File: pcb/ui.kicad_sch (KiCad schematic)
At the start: 10 parts, among them Q1 2N7002, Q13 BSS84, Q14 BSS84, Q15 BSS84, Q16 BSS84, U18 NHD-C12864A1Z-FSW-FBW-HTT, U21 74LVC1G139, U23 74LVC1G139, U24 TLC5927IPWPR

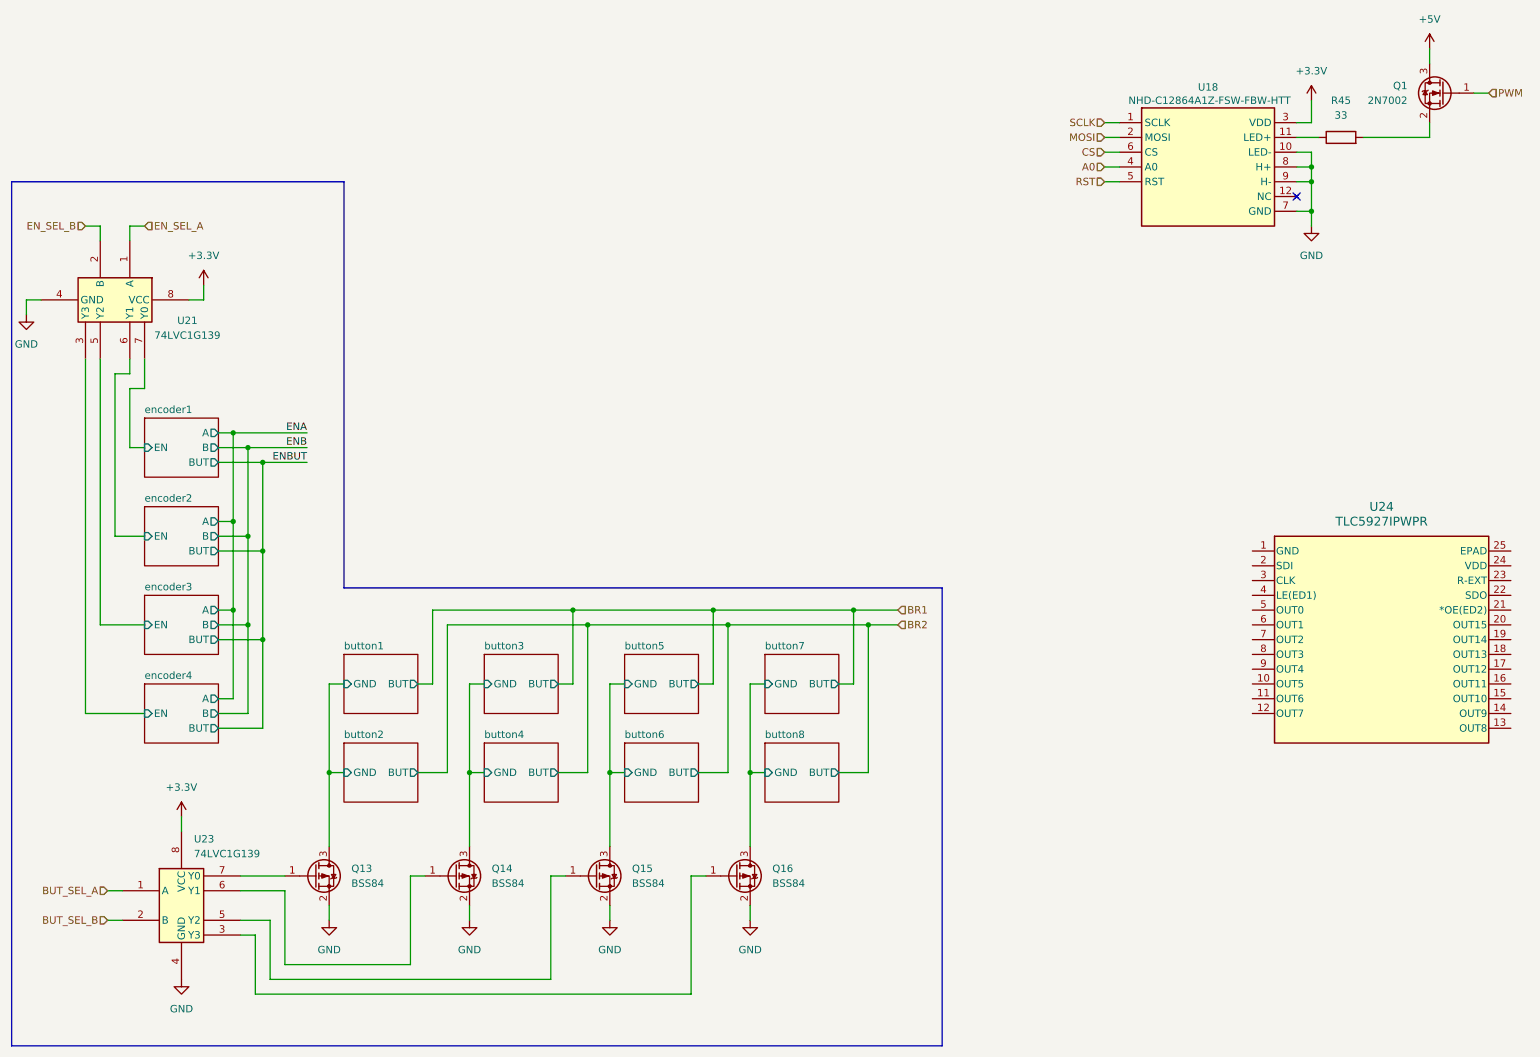
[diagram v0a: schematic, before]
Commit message: refactor: removed the laser component of the project
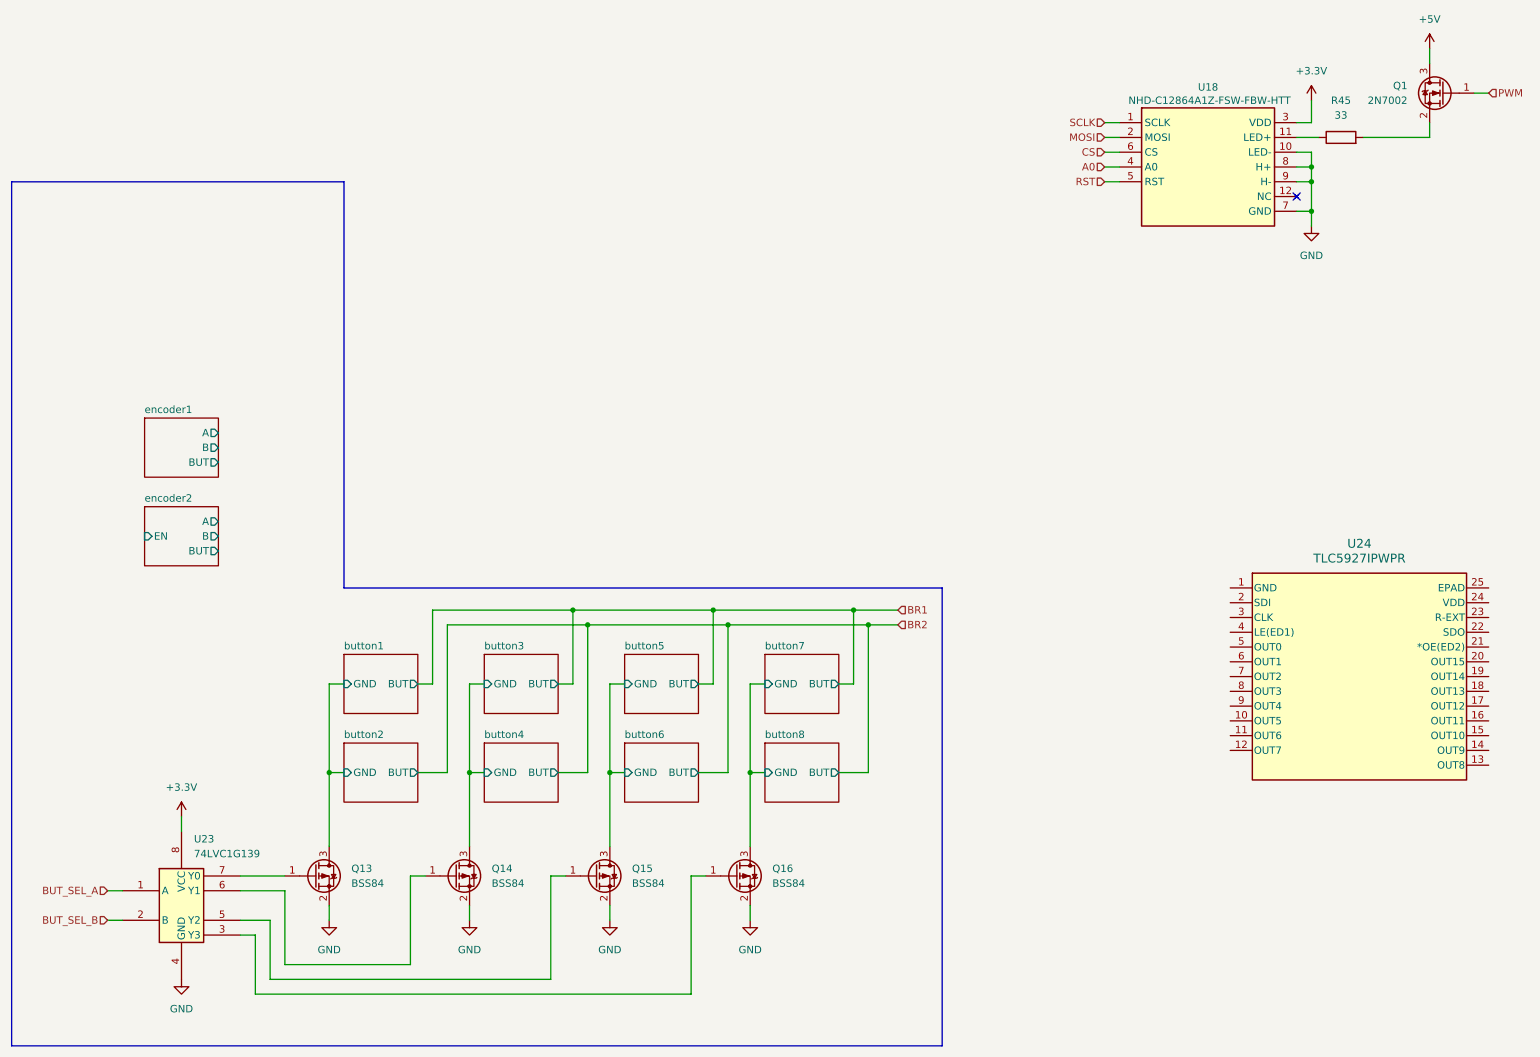
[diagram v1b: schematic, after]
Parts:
- removed U21: 74LVC1G139, symbol 74xGxx:74LVC1G139
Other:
- removed sheet encoder3
- removed sheet encoder4
- sheet encoder1 ports: added none; removed EN
- moved on the sheet: U24
